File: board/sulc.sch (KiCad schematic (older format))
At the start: 54 parts

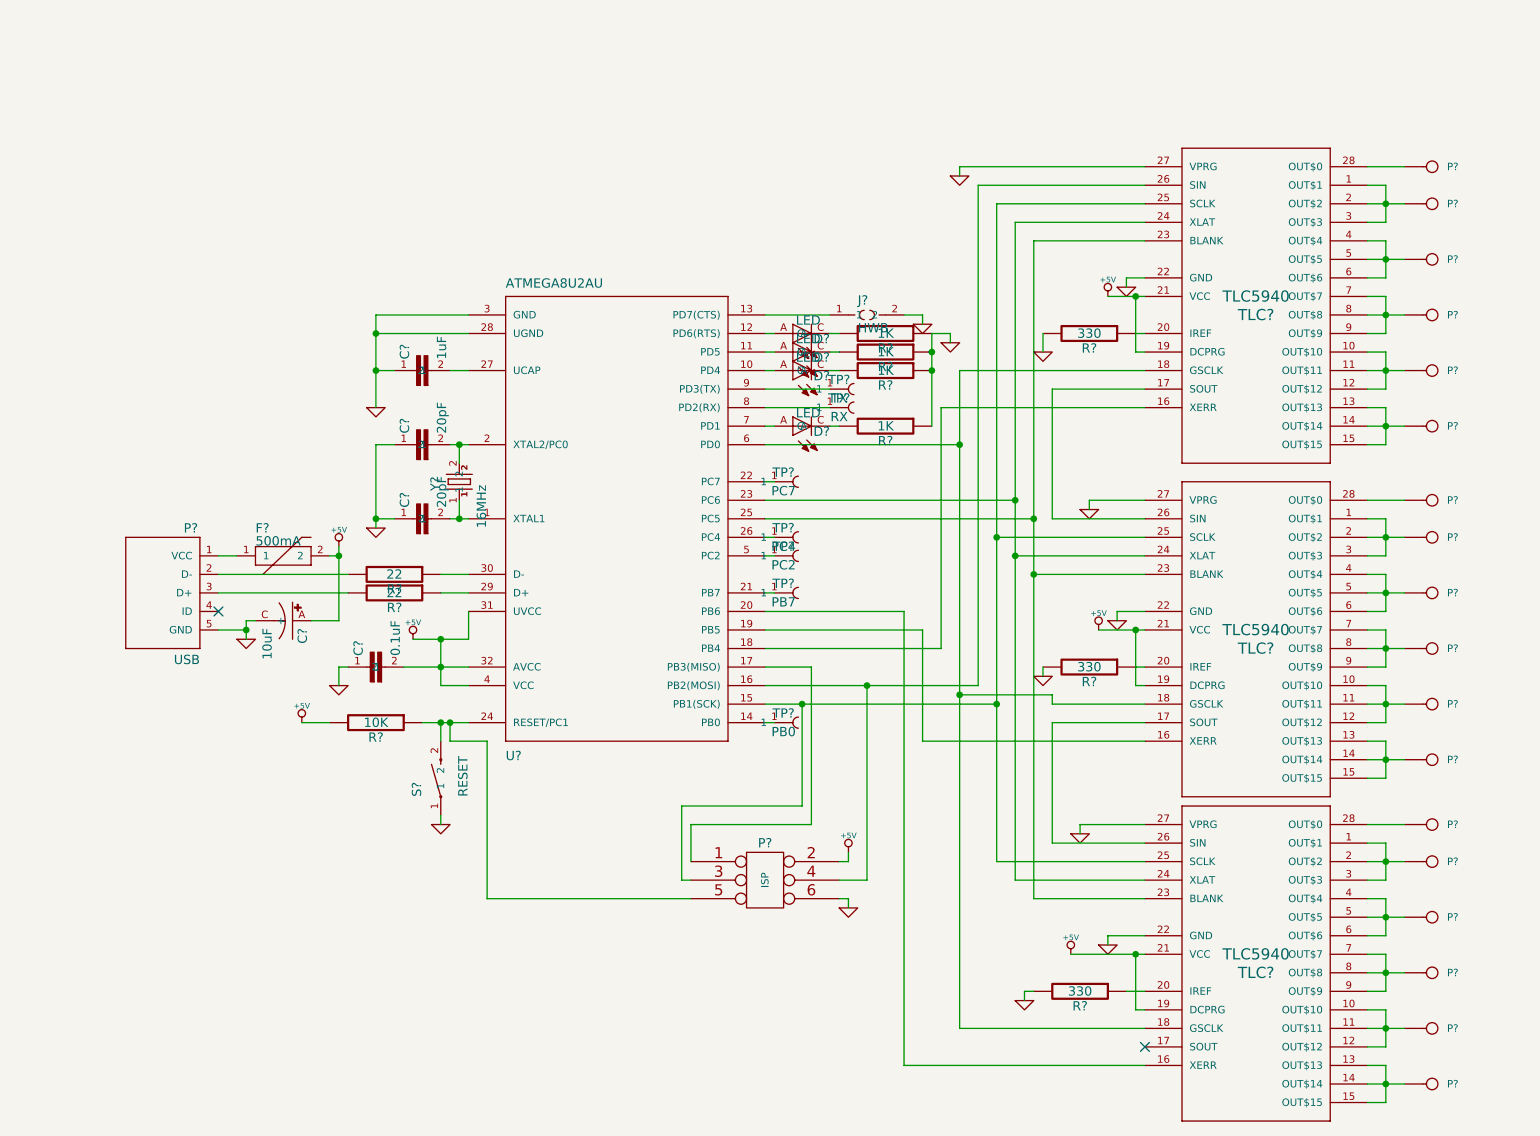
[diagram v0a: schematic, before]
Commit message: Added barrel jack for LED power
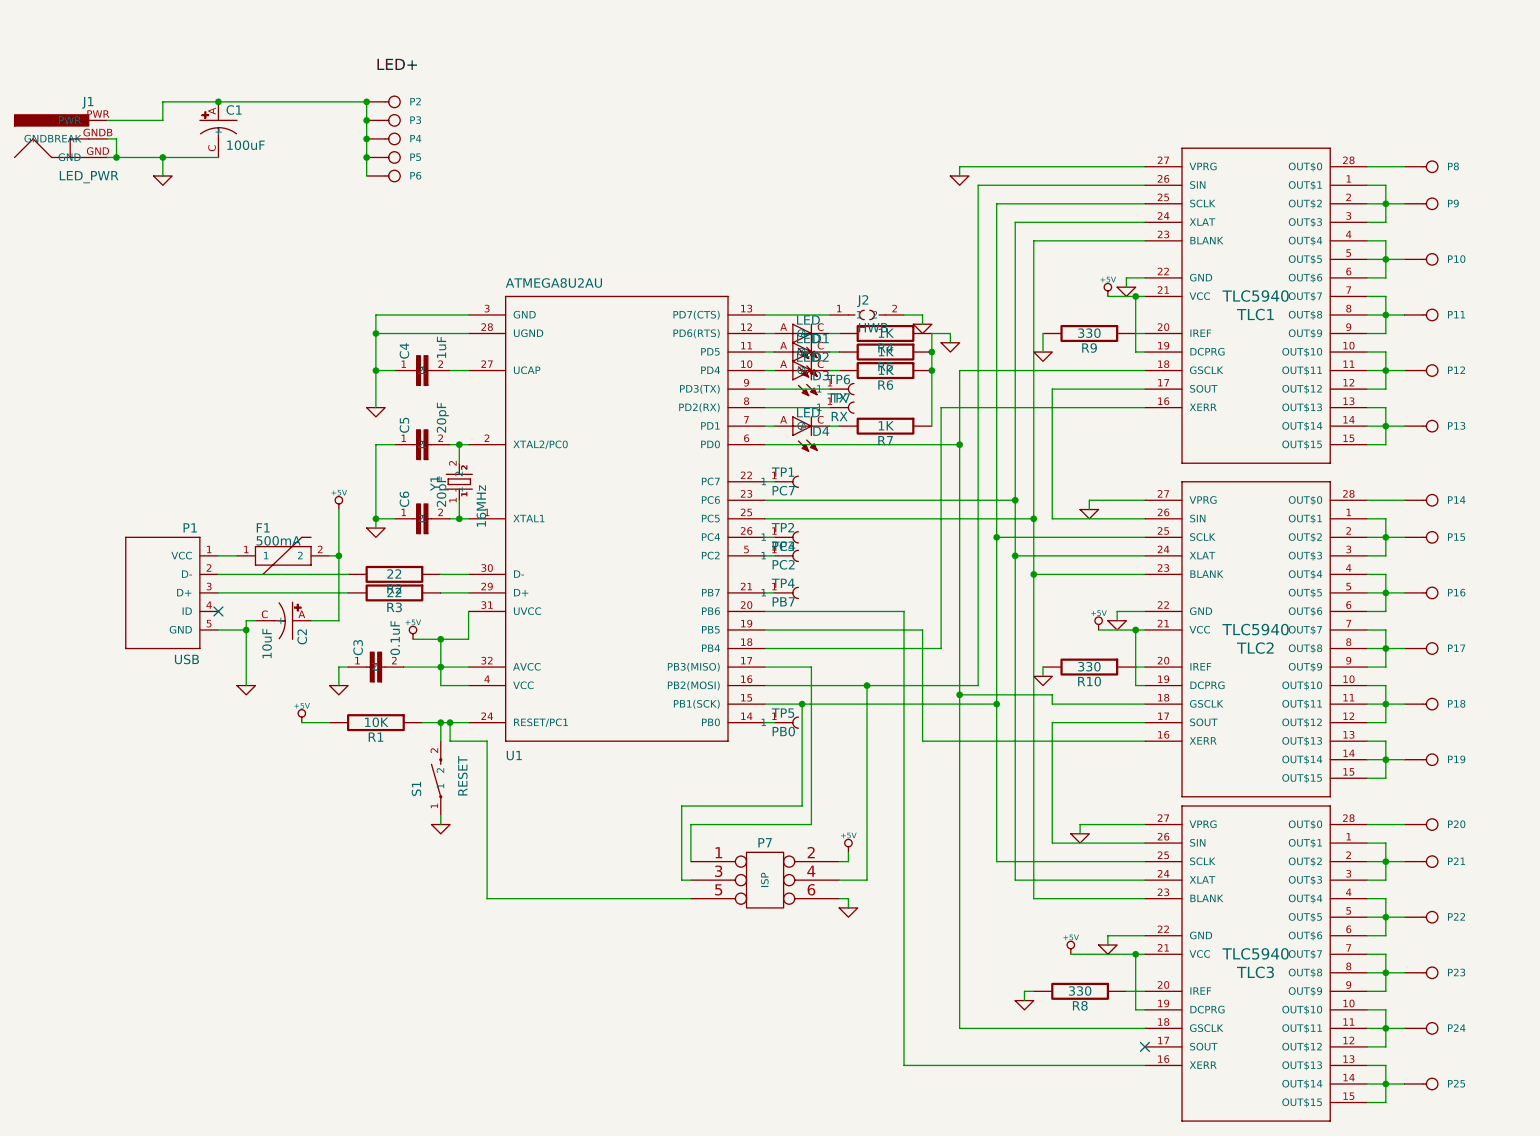
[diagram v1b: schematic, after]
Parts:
- added C1: 100uF, SparkFun-EIA7343, symbol CAP_POL7343
- added J1: LED_PWR, SparkFun-POWER_JACK_PTH, symbol POWER_JACKPTH
- added P2, P3, P4, P5, P6: CONN_1, symbol CONN_1
- gave numbers to parts that had none: 54
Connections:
- net GND: now also C1.C (-), J1.GND, J1.GNDB (GNDBREAK)
- new net: C1.A (+), J1.PWR, P2.1, P3.1, P4.1, P5.1, P6.1

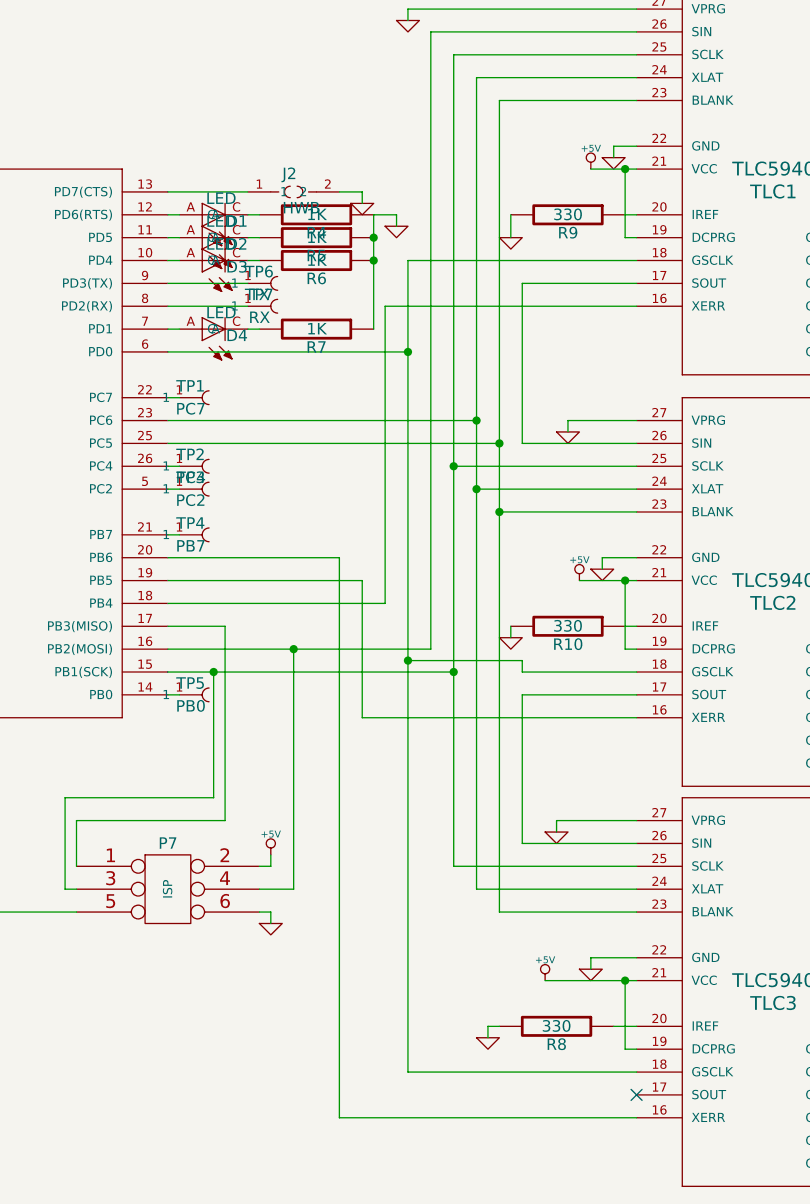
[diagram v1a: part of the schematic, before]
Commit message: Connect SOUT to MISO; solder bridges on SPI pins
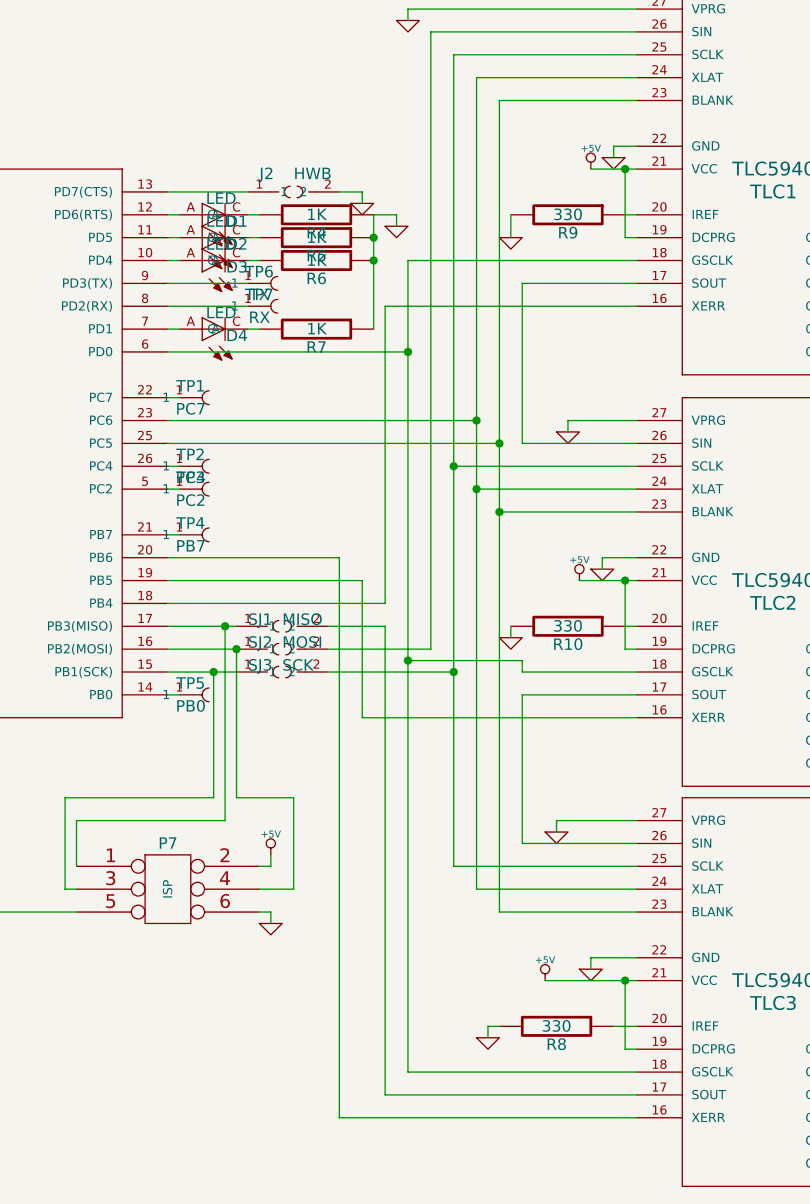
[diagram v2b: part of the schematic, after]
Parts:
- added SJ1: MISO, SparkFun-SJ_2S-NO, symbol SOLDERJUMPERNO
- added SJ2: MOSI, SparkFun-SJ_2S-NO, symbol SOLDERJUMPERNO
- added SJ3: SCK, SparkFun-SJ_2S-NO, symbol SOLDERJUMPERNO
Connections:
- net at TLC1.25 (SCLK), TLC2.25 (SCLK), TLC3.25 (SCLK): now also SJ3.2; no longer P7.3, U1.15 (PB1(SCK))
- net at P7.4, U1.16 (PB2(MOSI)): now also SJ2.1; no longer TLC1.26 (SIN)
- net at P7.1, U1.17 (PB3(MISO)): now also SJ1.1
- net at TLC3.17 (SOUT): now also SJ1.2
- new net: P7.3, SJ3.1, U1.15 (PB1(SCK))
- new net: SJ2.2, TLC1.26 (SIN)
- no-connect marks 2 -> 1
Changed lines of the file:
@@
-EESchema Schematic File Version 2  date Saturday, February 11, 2012 05:10:42 PM
+EESchema Schematic File Version 2  date Saturday, February 11, 2012 10:38:35 PM
 LIBS:power
 LIBS:device
@@
 Sheet 1 1
 Title "SULC - Simple USB LED Controller"
-Date "11 feb 2012"
+Date "12 feb 2012"
 Rev ""
 Comp "Scott Bezek (scottbezek.com)"
@@
 Comment4 ""
 $EndDescr
-Text Label 3250 850  0    60   ~ 0
-LED+
+Connection ~ 5650 4150
+Wire Wire Line
+	5650 4800 5650 4150
+Wire Wire Line
+	5650 4800 5900 4800
+Wire Wire Line
+	5900 4800 5900 5200
+Connection ~ 5600 4050
+Wire Wire Line
+	5650 4050 5350 4050
+Wire Wire Line
+	5650 4150 5350 4150
+Wire Wire Line
+	5650 4250 5350 4250
 Connection ~ 3200 1000
 Connection ~ 3200 1300
@@
 Wire Wire Line
 	3650 4450 3650 4350
-Connection ~ 5900 4150
-Wire Wire Line
-	5750 5200 5900 5200
-Wire Wire Line
-	5900 5200 5900 4150
+Wire Wire Line
+	5900 5200 5750 5200
 Wire Wire Line
 	4950 5200 4900 5200
@@
 	4950 4900 5600 4900
 Wire Wire Line
-	5350 4050 5600 4050
-Wire Wire Line
 	5350 3650 5400 3650
 Wire Wire Line
@@
 Wire Wire Line
 	5400 2350 5350 2350
-Wire Wire Line
-	5350 4250 6600 4250
 Wire Wire Line
 	5350 3950 6300 3950
@@
 	6200 3850 5350 3850
 Wire Wire Line
-	6500 4150 5350 4150
-Wire Wire Line
 	5350 2250 5400 2250
 Wire Wire Line
@@
 	5800 5100 5800 5050
 Wire Wire Line
-	5600 4050 5600 4900
+	5600 4900 5600 4050
 Wire Wire Line
 	5750 5300 5800 5300
@@
 	2100 1100 2100 1000
 Connection ~ 3200 1200
+Wire Wire Line
+	6050 4250 6600 4250
+Wire Wire Line
+	6500 4150 6050 4150
+Wire Wire Line
+	7400 6100 6300 6100
+Wire Wire Line
+	6300 6100 6300 4050
+Wire Wire Line
+	6300 4050 6050 4050
+$Comp
+L SOLDERJUMPERNO SJ1
+U 1 1 4F3732E8
+P 5850 4050
+F 0 "SJ1" H 5700 4050 50  0000 L BNN
+F 1 "MISO" H 5850 4050 50  0000 L BNN
+F 2 "SparkFun-SJ_2S-NO" H 5850 3850 50  0001 C CNN
+	1    5850 4050
+	1    0    0    -1
+$EndComp
+$Comp
+L SOLDERJUMPERNO SJ3
+U 1 1 4F37325E
+P 5850 4250
+F 0 "SJ3" H 5700 4250 50  0000 L BNN
+F 1 "SCK" H 5850 4250 50  0000 L BNN
+F 2 "SparkFun-SJ_2S-NO" H 5850 4050 50  0001 C CNN
+	1    5850 4250
+	1    0    0    -1
+$EndComp
+$Comp
+L SOLDERJUMPERNO SJ2
+U 1 1 4F37321A
+P 5850 4150
+F 0 "SJ2" H 5700 4150 50  0000 L BNN
+F 1 "MOSI" H 5850 4150 50  0000 L BNN
+F 2 "SparkFun-SJ_2S-NO" H 5850 3950 50  0001 C CNN
+	1    5850 4150
+	1    0    0    -1
+$EndComp
+Text Label 3250 850  0    60   ~ 0
+LED+
 $Comp
 L CONN_1 P6
@@
 $EndComp
 $Comp
-L GND #PWR1
+L GND #PWR01
 U 1 1 4F36E5C2
 P 2100 1400
-F 0 "#PWR1" H 2100 1400 30  0001 C CNN
+F 0 "#PWR01" H 2100 1400 30  0001 C CNN
 F 1 "GND" H 2100 1330 30  0001 C CNN
 	1    2100 1400
@@
 $EndComp
 $Comp
-L GND #PWR2
+L GND #PWR02
 U 1 1 4F36E2C9
 P 2550 4150
-F 0 "#PWR2" H 2550 4150 30  0001 C CNN
+F 0 "#PWR02" H 2550 4150 30  0001 C CNN
 F 1 "GND" H 2550 4080 30  0001 C CNN
 	1    2550 4150
@@
 $EndComp
 $Comp
-L +5V #PWR4
+L +5V #PWR03
 U 1 1 4F36E2B1
 P 3050 3200
-F 0 "#PWR4" H 3050 3290 20  0001 C CNN
+F 0 "#PWR03" H 3050 3290 20  0001 C CNN
 F 1 "+5V" H 3050 3290 30  0000 C CNN
 	1    3050 3200
@@
 $EndComp
 $Comp
-L GND #PWR5
+L GND #PWR04
 U 1 1 4F36DCF3
 P 3050 4150
-F 0 "#PWR5" H 3050 4150 30  0001 C CNN
+F 0 "#PWR04" H 3050 4150 30  0001 C CNN
 F 1 "GND" H 3050 4080 30  0001 C CNN
 	1    3050 4150
@@
 $EndComp
 $Comp
-L GND #PWR11
+L GND #PWR05
 U 1 1 4F36DB3E
 P 5800 5350
-F 0 "#PWR11" H 5800 5350 30  0001 C CNN
+F 0 "#PWR05" H 5800 5350 30  0001 C CNN
 F 1 "GND" H 5800 5280 30  0001 C CNN
 	1    5800 5350
@@
 $EndComp
 $Comp
-L +5V #PWR10
+L +5V #PWR06
 U 1 1 4F36DAF0
 P 5800 5050
-F 0 "#PWR10" H 5800 5140 20  0001 C CNN
+F 0 "#PWR06" H 5800 5140 20  0001 C CNN
 F 1 "+5V" H 5800 5140 30  0000 C CNN
 	1    5800 5050
@@
 $EndComp
 $Comp
-L GND #PWR13
+L GND #PWR07
 U 1 1 4F36D62B
 P 6350 2300
-F 0 "#PWR13" H 6350 2300 30  0001 C CNN
+F 0 "#PWR07" H 6350 2300 30  0001 C CNN
 F 1 "GND" H 6350 2230 30  0001 C CNN
 	1    6350 2300
@@
 U 1 1 4F36D089
 P 5900 2150
-F 0 "J2" H 5850 2200 50  0000 L BNN
-F 1 "HWB" H 5850 2050 50  0000 L BNN
+F 0 "J2" H 5750 2200 50  0000 L BNN
+F 1 "HWB" H 5900 2200 50  0000 L BNN
 F 2 "SparkFun-SJ_2S" H 5900 1950 50  0001 C CNN
 	1    5900 2150
@@
 $EndComp
 $Comp
-L GND #PWR23
+L GND #PWR08
 U 1 1 4F36C48C
 P 7200 5550
-F 0 "#PWR23" H 7200 5550 30  0001 C CNN
+F 0 "#PWR08" H 7200 5550 30  0001 C CNN
 F 1 "GND" H 7200 5480 30  0001 C CNN
 	1    7200 5550
 	1    0    0    -1
 $EndComp
-NoConn ~ 7400 6100
-$Comp
-L GND #PWR15
+$Comp
+L GND #PWR09
 U 1 1 4F36C451
 P 6750 5850
-F 0 "#PWR15" H 6750 5850 30  0001 C CNN
+F 0 "#PWR09" H 6750 5850 30  0001 C CNN
 F 1 "GND" H 6750 5780 30  0001 C CNN
 	1    6750 5850
@@
 $EndComp
 $Comp
-L +5V #PWR18
+L +5V #PWR010
 U 1 1 4F36C440
 P 7000 5600
-F 0 "#PWR18" H 7000 5690 20  0001 C CNN
+F 0 "#PWR010" H 7000 5690 20  0001 C CNN
 F 1 "+5V" H 7000 5690 30  0000 C CNN
 	1    7000 5600
@@
 $EndComp
 $Comp
-L GND #PWR19
+L GND #PWR011
 U 1 1 4F36C437
 P 7050 4950
-F 0 "#PWR19" H 7050 4950 30  0001 C CNN
+F 0 "#PWR011" H 7050 4950 30  0001 C CNN
 F 1 "GND" H 7050 4880 30  0001 C CNN
 	1    7050 4950
@@
 $EndComp
 $Comp
-L GND #PWR24
+L GND #PWR012
 U 1 1 4F36C41C
 P 7250 3800
-F 0 "#PWR24" H 7250 3800 30  0001 C CNN
+F 0 "#PWR012" H 7250 3800 30  0001 C CNN
 F 1 "GND" H 7250 3730 30  0001 C CNN
 	1    7250 3800
@@
 $EndComp
 $Comp
-L +5V #PWR21
+L +5V #PWR013
 U 1 1 4F36C3DE
 P 7150 3850
-F 0 "#PWR21" H 7150 3940 20  0001 C CNN
+F 0 "#PWR013" H 7150 3940 20  0001 C CNN
 F 1 "+5V" H 7150 3940 30  0000 C CNN
 	1    7150 3850
@@
 $EndComp
 $Comp
-L GND #PWR17
+L GND #PWR014
 U 1 1 4F36C3D1
 P 6850 4100
-F 0 "#PWR17" H 6850 4100 30  0001 C CNN
+F 0 "#PWR014" H 6850 4100 30  0001 C CNN
 F 1 "GND" H 6850 4030 30  0001 C CNN
 	1    6850 4100
@@
 $EndComp
 $Comp
-L GND #PWR25
+L GND #PWR015
 U 1 1 4F36BF6A
 P 7300 2000
-F 0 "#PWR25" H 7300 2000 30  0001 C CNN
+F 0 "#PWR015" H 7300 2000 30  0001 C CNN
 F 1 "GND" H 7300 1930 30  0001 C CNN
 	1    7300 2000
@@
 $EndComp
 $Comp
-L +5V #PWR22
+L +5V #PWR016
 U 1 1 4F36BF4A
 P 7200 2050
-F 0 "#PWR22" H 7200 2140 20  0001 C CNN
+F 0 "#PWR016" H 7200 2140 20  0001 C CNN
 F 1 "+5V" H 7200 2140 30  0000 C CNN
 	1    7200 2050
@@
 $EndComp
 $Comp
-L GND #PWR20
+L GND #PWR017
 U 1 1 4F36BF2F
 P 7100 3200
-F 0 "#PWR20" H 7100 3200 30  0001 C CNN
+F 0 "#PWR017" H 7100 3200 30  0001 C CNN
 F 1 "GND" H 7100 3130 30  0001 C CNN
 	1    7100 3200
@@
 $EndComp
 $Comp
-L GND #PWR14
+L GND #PWR018
 U 1 1 4F36BF18
 P 6400 1400
-F 0 "#PWR14" H 6400 1400 30  0001 C CNN
+F 0 "#PWR018" H 6400 1400 30  0001 C CNN
 F 1 "GND" H 6400 1330 30  0001 C CNN
 	1    6400 1400
@@
 $EndComp
 $Comp
-L GND #PWR16
+L GND #PWR019
 U 1 1 4F36BEDF
 P 6850 2350
-F 0 "#PWR16" H 6850 2350 30  0001 C CNN
+F 0 "#PWR019" H 6850 2350 30  0001 C CNN
 F 1 "GND" H 6850 2280 30  0001 C CNN
 	1    6850 2350
@@
 $EndComp
 $Comp
-L GND #PWR9
+L GND #PWR020
 U 1 1 4F36BDDE
 P 3600 4900
-F 0 "#PWR9" H 3600 4900 30  0001 C CNN
+F 0 "#PWR020" H 3600 4900 30  0001 C CNN
 F 1 "GND" H 3600 4830 30  0001 C CNN
 	1    3600 4900
@@
 $EndComp
 $Comp
-L +5V #PWR3
+L +5V #PWR021
 U 1 1 4F36BDC4
 P 2850 4350
-F 0 "#PWR3" H 2850 4440 20  0001 C CNN
+F 0 "#PWR021" H 2850 4440 20  0001 C CNN
 F 1 "+5V" H 2850 4440 30  0000 C CNN
 	1    2850 4350
@@
 $EndComp
 $Comp
-L GND #PWR12
+L GND #PWR022
 U 1 1 4F35DDEF
 P 6200 2200
-F 0 "#PWR12" H 6200 2200 30  0001 C CNN
+F 0 "#PWR022" H 6200 2200 30  0001 C CNN
 F 1 "GND" H 6200 2130 30  0001 C CNN
 	1    6200 2200
@@
 $EndComp
 $Comp
-L +5V #PWR8
+L +5V #PWR023
 U 1 1 4F35DD77
 P 3450 3900
-F 0 "#PWR8" H 3450 3990 20  0001 C CNN
+F 0 "#PWR023" H 3450 3990 20  0001 C CNN
 F 1 "+5V" H 3450 3990 30  0000 C CNN
 	1    3450 3900
@@
 $EndComp
 $Comp
-L GND #PWR7
+L GND #PWR024
 U 1 1 4F35DD45
 P 3250 3300
-F 0 "#PWR7" H 3250 3300 30  0001 C CNN
+F 0 "#PWR024" H 3250 3300 30  0001 C CNN
 F 1 "GND" H 3250 3230 30  0001 C CNN
 	1    3250 3300
@@
 $EndComp
 $Comp
-L GND #PWR6
+L GND #PWR025
 U 1 1 4F35DCA1
 P 3250 2650
-F 0 "#PWR6" H 3250 2650 30  0001 C CNN
+F 0 "#PWR025" H 3250 2650 30  0001 C CNN
 F 1 "GND" H 3250 2580 30  0001 C CNN
 	1    3250 2650

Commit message: Preliminary PCB design
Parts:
- added D5: PWR, SparkFun-LED-1206, symbol LED1206
- added R11: 1K, symbol R
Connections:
- net +5V: now also D5.A
- net GND: now also R11.2
- new net: D5.C, R11.1

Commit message: TSSOP28, silkscreen changes
- Removed holes under solder paste for TSSOP28 to avoid solder being wicked away
- Removed silkscreen overhanging board boundary
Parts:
- F1: digikey (none) -> NANOSMDC050F/13.2CT-ND
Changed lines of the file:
@@
-EESchema Schematic File Version 2  date Sunday, February 12, 2012 10:45:52 PM
+EESchema Schematic File Version 2  date Monday, February 13, 2012 07:53:14 PM
 LIBS:power
 LIBS:device
@@
 Sheet 1 1
 Title "SULC - Simple USB LED Controller"
-Date "12 feb 2012"
+Date "14 feb 2012"
 Rev ""
 Comp "Scott Bezek (scottbezek.com)"
@@
 F 1 "500mA" H 2600 3500 50  0000 L BNN
 F 2 "SparkFun-PTC-1206" H 2700 3600 50  0001 C CNN
+F 4 "NANOSMDC050F/13.2CT-ND" H 2700 3450 60  0001 C CNN "digikey"
 	1    2700 3450
 	1    0    0    -1
